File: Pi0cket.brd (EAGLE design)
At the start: 55.9 x 64.8 mm, 13 parts, among them T1 SI2301, U1 Tiny85-20-SMT

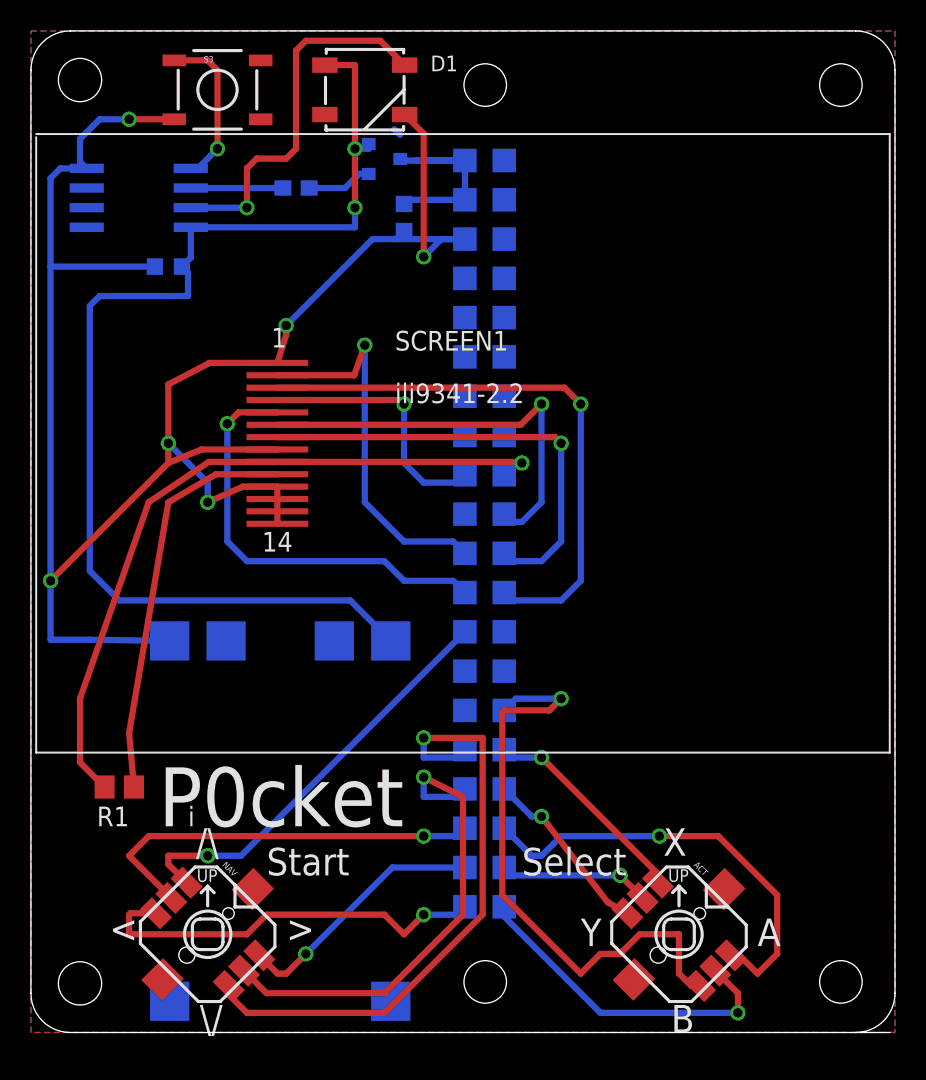
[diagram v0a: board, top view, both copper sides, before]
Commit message: some tweaks
added i2c lines from the attiny to the pi (might live to regret that!!)

re-arranged the tiny and associated bits to make things flow better

added battery socket back in for ease of external charging

moved backlight resistor to save some space
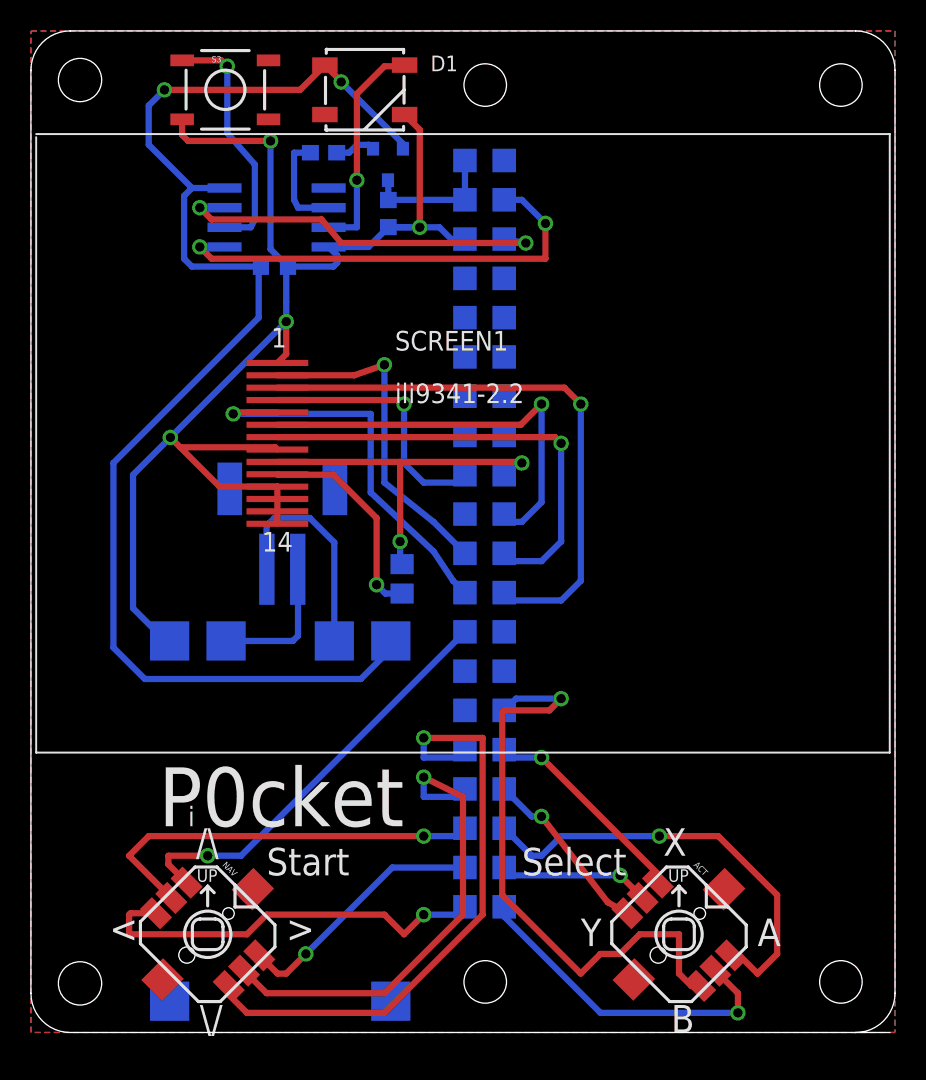
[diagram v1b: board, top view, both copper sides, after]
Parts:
- added CN1: (no value), adafruit:JST-PH-2-SMT-RA
- moved R1 22.7 mm to (25.3, 30.6), flipped to the bottom, turned to 90 degrees
- moved U1 8.98 mm to (17.1, 54.0), turned to 270 degrees
- moved C1 6.86 mm to (17.0, 50.8), turned to 180 degrees
- moved R2 2.90 mm to (20.2, 58.2)
- moved C3 1.05 mm to (24.4, 54.2)
- moved S3 0.51 mm to (13.8, 62.2)
- moved T1 0.46 mm to (24.4, 57.4), turned to 0 degrees
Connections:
- new net N$16: S3.1, U1.6
- new net N$20: R2.1, U1.2
- new net N$26: D1.4, U1.3
- new net N$29: CN1.2, POWER1.B-
- net N$24: now also CN1.1, POWER1.B+; no longer R2.1, U1.6
- net N$25: now also PI1.3; no longer S3.1
- net N$28: now also PI1.5; no longer D1.4
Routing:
- net GND: track 128.0 -> 88.8 mm, vias 6 -> 4
- net N$19: track 46.2 -> 24.0 mm, vias 1 -> 2
- net N$25: track 10.4 -> 29.9 mm, vias 1 -> 2
- net N$16: track 0.00 -> 15.9 mm, vias 0 -> 1
- net N$26: track 0.00 -> 14.3 mm, vias 0 -> 1
- net N$27: track 74.2 -> 87.2 mm
- net N$5: track 26.2 -> 13.8 mm, vias 0 -> 1
- net N$29: track 0.00 -> 9.10 mm
- net N$24: track 5.96 -> 14.4 mm
- net N$20: track 0.00 -> 6.65 mm
- net 5V0@2: track 14.6 -> 8.79 mm
- net N$1: track 25.0 -> 21.6 mm
- net N$7: track 27.9 -> 25.8 mm
- net N$21: track 4.23 -> 2.67 mm
- net N$28: track 24.2 -> 25.1 mm, vias 1 -> 2
